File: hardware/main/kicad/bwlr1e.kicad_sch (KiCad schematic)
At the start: 62 parts, among them J1 Qwiic, Q1 AO3407A, Q2 DMG1012UW, SW3 RESET, SW4 BOOT, U1 BME688, U2 RAK3172-T, U3 AEM10941, U4 XC6215

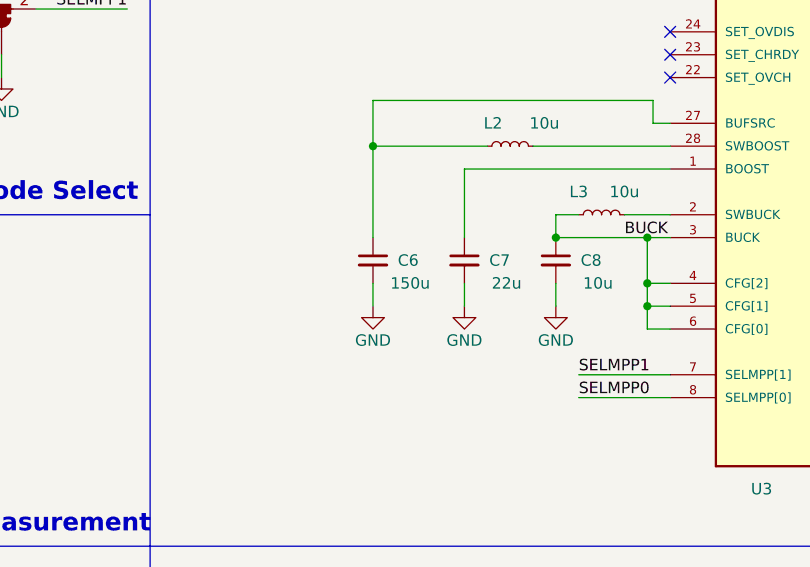
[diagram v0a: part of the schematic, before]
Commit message: change csrc aem10941 to 10uf
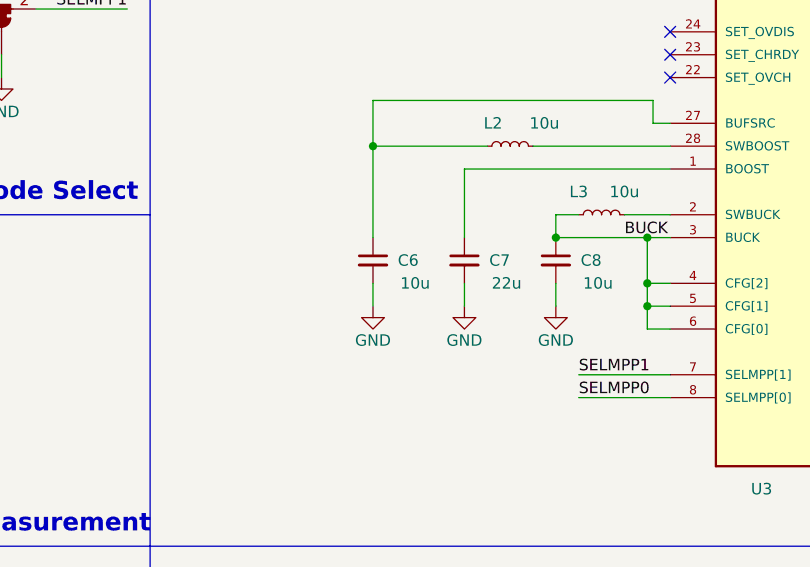
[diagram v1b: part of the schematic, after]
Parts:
- C6: value 150u -> 10u; footprint Capacitor_SMD:C_1210_3225Metric -> Capacitor_SMD:C_0603_1608Metric; Part Description Ceramic Capacitor 150uF 20% 6.3V X5R -> Ceramic Capacitor 10uF 10% 10V X5R
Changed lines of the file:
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@@
   (title_block
     (title "Teapotlabs BWLR1E")
-    (date "2023-08-12")
-    (rev "4")
+    (date "2023-09-26")
+    (rev "5")
     (company "Teapot Laboratories")
   )
@@
       (effects (font (size 1.27 1.27)) (justify right))
     )
-    (property "Value" "150u" (at 193.04 58.42 0)
+    (property "Value" "10u" (at 193.04 58.42 0)
       (effects (font (size 1.27 1.27)) (justify right))
     )
-    (property "Footprint" "Capacitor_SMD:C_1210_3225Metric" (at 186.69 55.88 0)
+    (property "Footprint" "Capacitor_SMD:C_0603_1608Metric" (at 186.69 55.88 0)
       (effects (font (size 1.27 1.27)) hide)
     )
@@
       (effects (font (size 1.27 1.27)) hide)
     )
-    (property "Part Description" "Ceramic Capacitor 150uF 20% 6.3V X5R" (at 186.69 55.88 0)
-      (effects (font (size 1.27 1.27)) hide)
-    )
+    (property "Part Description" "Ceramic Capacitor 10uF 10% 10V X5R" (at 186.69 55.88 0)
+      (effects (font (size 1.27 1.27)) hide)
+    )
+    (property "Manufacturer" "" (at 186.69 55.88 0)
+      (effects (font (size 1.27 1.27)) hide)
+    )
+    (property "Manufacturer Part Number" "" (at 186.69 55.88 0)
+      (effects (font (size 1.27 1.27)) hide)
+    )
+    (property "Distributor" "" (at 186.69 55.88 0)
+      (effects (font (size 1.27 1.27)) hide)
+    )
+    (property "Distributor Part Number" "" (at 186.69 55.88 0)
+      (effects (font (size 1.27 1.27)) hide)
+    )
+    (property "Distributor Link" "" (at 186.69 55.88 0)
+      (effects (font (size 1.27 1.27)) hide)
+    )
